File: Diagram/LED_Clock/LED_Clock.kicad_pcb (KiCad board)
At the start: 2 copper layers, 190.5 x 159.4 mm, 79 parts, among them SW1 SW_Push_Dual, U1 ATmega328P-PU, U2 DS3231MZ, U3 MCP23017-E_SP, U4 MCP23017-E_SP, U5 Barreljack, U6 JST4pin, Y1 Crystal

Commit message: Ground Plane
added a Ground plane and some missing traces.
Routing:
- net Net-(D9-Pad1): track 0.00 -> 10.2 mm
- net Net-(D8-Pad1): track 0.00 -> 10.2 mm
- net Net-(D7-Pad1): track 0.00 -> 10.2 mm
- net Net-(D6-Pad1): track 0.00 -> 10.2 mm
- net Net-(D5-Pad1): track 0.00 -> 10.2 mm
- net Net-(D15-Pad1): track 0.00 -> 10.2 mm
- net Net-(D14-Pad1): track 0.00 -> 10.2 mm
- net Net-(D13-Pad1): track 0.00 -> 10.2 mm
- net Net-(D12-Pad1): track 0.00 -> 10.2 mm
- net Net-(D11-Pad1): track 0.00 -> 10.2 mm
- net Net-(D10-Pad1): track 0.00 -> 10.2 mm
- added copper zone on F.Cu, net GND

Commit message: updated
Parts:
- moved R1 34.9 mm to (84.8, 128.5), turned to 270 degrees
- moved SW1 28.5 mm to (77.2, 131.6)
- moved REF** 25.3 mm to (60.5, 146.8)
- moved U5 23.6 mm to (58.9, 130.6)
- moved U1 22.5 mm to (144.3, 108.7)
- moved Y1 22.0 mm to (138.2, 130.6)
- moved REF** 21.0 mm to (214.4, 146.8)
- moved C1 20.8 mm to (133.1, 133.1)
- moved C2 20.7 mm to (133.1, 128.0)
- moved R2 20.0 mm to (158.2, 110.7)
- moved R3 20.0 mm to (158.2, 115.8)
- moved REF** 19.8 mm to (177.6, 129.0)
- moved REF** 19.8 mm to (177.5, 122.0)
- moved U2 19.8 mm to (159.8, 124.7)
- moved REF** 19.6 mm to (60.5, 29.5)
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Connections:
- net GPB1 renamed Net-(R16-Pad2)
- R15 pad 2: GPB0 -> Net-(R15-Pad2)
- R17 pad 2: GPB2 -> Net-(R17-Pad2)
- R18 pad 2: GPB3 -> Net-(R18-Pad2)
- R19 pad 2: GPB4 -> Net-(R19-Pad2)
- R20 pad 2: GPB5 -> Net-(R20-Pad2)
- R21 pad 2: GPB6 -> Net-(R21-Pad2)
- R30 pad 2: HGPB0 -> Net-(R30-Pad2)
- R31 pad 2: HGPB1 -> Net-(R31-Pad2)
- R32 pad 2: HGPB2 -> Net-(R32-Pad2)
- R33 pad 2: HGPB3 -> Net-(R33-Pad2)
- U1 pad 16: Net-(U1-Pad16) -> +5V
- U1 pad 18: Net-(U1-Pad18) -> GND
- U3 pad 1: GPB0 -> Net-(R17-Pad2)
- U3 pad 21: Net-(R7-Pad2) -> Net-(R10-Pad2)
- U3 pad 22: Net-(R8-Pad2) -> Net-(R9-Pad2)
- U3 pad 23: Net-(R9-Pad2) -> Net-(R8-Pad2)
- U3 pad 24: Net-(R10-Pad2) -> Net-(R7-Pad2)
- U3 pad 25: Net-(R11-Pad2) -> Net-(R21-Pad2)
- U3 pad 26: Net-(R12-Pad2) -> Net-(R20-Pad2)
- U3 pad 27: Net-(R13-Pad2) -> Net-(R19-Pad2)
- U3 pad 28: Net-(R14-Pad2) -> Net-(R18-Pad2)
- U3 pad 3: GPB2 -> Net-(R15-Pad2)
- U3 pad 4: GPB3 -> Net-(R14-Pad2)
- U3 pad 5: GPB4 -> Net-(R13-Pad2)
- U3 pad 6: GPB5 -> Net-(R12-Pad2)
- U3 pad 7: GPB6 -> Net-(R11-Pad2)
- U4 pad 1: HGPB0 -> Net-(R25-Pad2)
- U4 pad 2: HGPB1 -> Net-(R24-Pad2)
- U4 pad 21: Net-(R22-Pad2) -> Net-(R33-Pad2)
- U4 pad 22: Net-(R23-Pad2) -> Net-(R32-Pad2)
- U4 pad 23: Net-(R24-Pad2) -> Net-(R31-Pad2)
- U4 pad 24: Net-(R25-Pad2) -> Net-(R30-Pad2)
- U4 pad 25: Net-(R26-Pad2) -> Net-(R29-Pad2)
- U4 pad 26: Net-(R27-Pad2) -> Net-(R28-Pad2)
- U4 pad 27: Net-(R28-Pad2) -> Net-(R27-Pad2)
- U4 pad 28: Net-(R29-Pad2) -> Net-(R26-Pad2)
- U4 pad 3: HGPB2 -> Net-(R23-Pad2)
- U4 pad 4: HGPB3 -> Net-(R22-Pad2)
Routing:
- net Net-(R33-Pad2): track 0.00 -> 172.7 mm
- net GND: track 1150.4 -> 982.4 mm
- net Net-(R32-Pad2): track 0.00 -> 158.5 mm
- net Net-(R21-Pad2): track 0.00 -> 151.5 mm
- net HGPB3: track 149.6 -> 0.00 mm
- net Net-(R31-Pad2): track 0.00 -> 144.4 mm
- net Net-(R20-Pad2): track 0.00 -> 137.4 mm
- net HGPB2: track 135.8 -> 0.00 mm
- net GPB6: track 130.3 -> 0.00 mm
- net Net-(R30-Pad2): track 0.00 -> 130.3 mm
- net /clock minute/SDA: track 261.5 -> 386.0 mm
- net Net-(R19-Pad2): track 0.00 -> 123.4 mm
- net HGPB1: track 122.0 -> 0.00 mm
- net GPB5: track 120.8 -> 0.00 mm
- net GPB2: track 115.4 -> 0.00 mm
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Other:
- board size 190.5 x 159.4 mm -> 164.1 x 127.5 mm
- rule pad_to_mask_clearance: 0.051 -> 0.00129
- rule solder_mask_min_width: 0.25 -> 0.002565
- rule trace_min: 0.2 -> 0.000152
- rule via_min_drill: 0.3 -> 0.000254
- rule via_min_size: 0.4 -> 0.000508

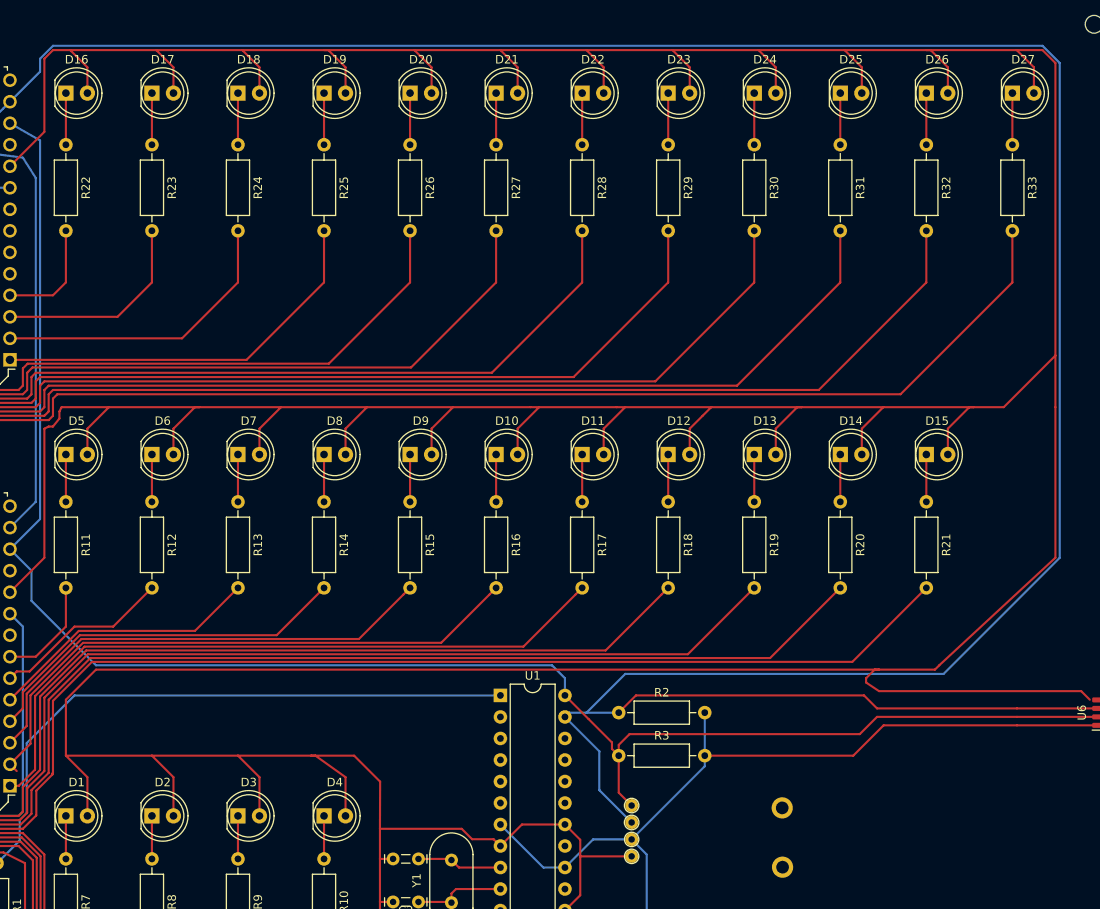
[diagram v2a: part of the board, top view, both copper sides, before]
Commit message: Updated
led flipped the RTS symbol remade and JST4pin enlarged
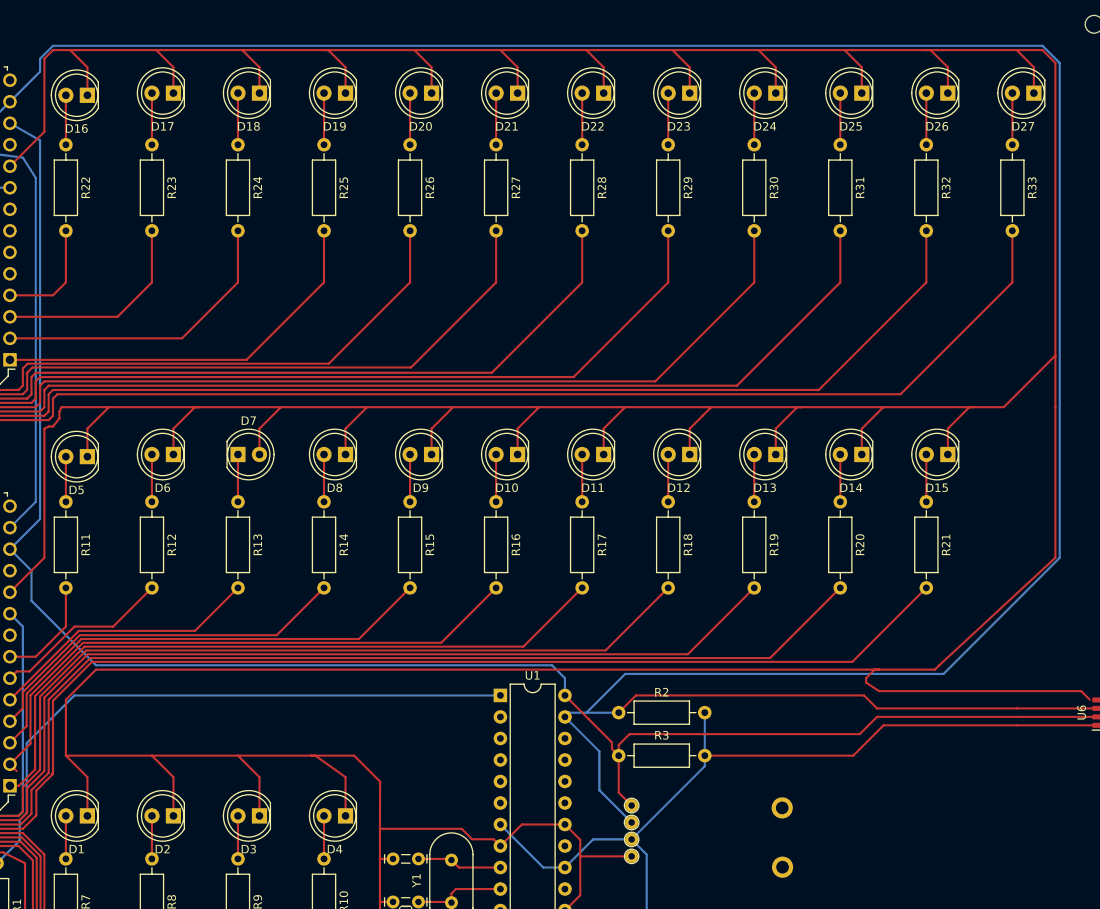
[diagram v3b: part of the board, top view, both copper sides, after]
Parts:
- moved D5 2.55 mm to (95.5, 80.5), turned to 180 degrees
- moved D16 2.55 mm to (95.5, 37.8), turned to 180 degrees
- moved D15 2.54 mm to (197.1, 80.3), turned to 180 degrees
- moved D26 2.54 mm to (197.1, 37.6), turned to 180 degrees
- moved D27 2.54 mm to (207.3, 37.6), turned to 180 degrees
- moved D1 2.54 mm to (95.5, 122.9), turned to 180 degrees
- moved D17 2.54 mm to (105.7, 37.6), turned to 180 degrees
- moved D2 2.54 mm to (105.7, 122.9), turned to 180 degrees
- moved D6 2.54 mm to (105.7, 80.3), turned to 180 degrees
- moved D10 2.54 mm to (146.3, 80.3), turned to 180 degrees
- moved D11 2.54 mm to (156.5, 80.3), turned to 180 degrees
- moved D12 2.54 mm to (166.6, 80.3), turned to 180 degrees
- moved D13 2.54 mm to (176.8, 80.3), turned to 180 degrees
- moved D14 2.54 mm to (186.9, 80.3), turned to 180 degrees
- moved D18 2.54 mm to (115.8, 37.6), turned to 180 degrees
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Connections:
- D1 pad 1: Net-(D1-Pad1) -> GND
- D1 pad 2: GND -> Net-(D1-Pad2)
- D10 pad 1: Net-(D10-Pad1) -> GND
- D10 pad 2: GND -> Net-(D10-Pad2)
- D11 pad 1: Net-(D11-Pad1) -> GND
- D11 pad 2: GND -> Net-(D11-Pad2)
- D12 pad 1: Net-(D12-Pad1) -> GND
- D12 pad 2: GND -> Net-(D12-Pad2)
- D13 pad 1: Net-(D13-Pad1) -> GND
- D13 pad 2: GND -> Net-(D13-Pad2)
- D14 pad 1: Net-(D14-Pad1) -> GND
- D14 pad 2: GND -> Net-(D14-Pad2)
- D15 pad 1: Net-(D15-Pad1) -> GND
- D15 pad 2: GND -> Net-(D15-Pad2)
- D16 pad 1: Net-(D16-Pad1) -> GND
- D16 pad 2: GND -> Net-(D16-Pad2)
- D17 pad 1: Net-(D17-Pad1) -> GND
- D17 pad 2: GND -> Net-(D17-Pad2)
- D18 pad 1: Net-(D18-Pad1) -> GND
- D18 pad 2: GND -> Net-(D18-Pad2)
- D19 pad 1: Net-(D19-Pad1) -> GND
- D19 pad 2: GND -> Net-(D19-Pad2)
- D2 pad 1: Net-(D2-Pad1) -> GND
- D2 pad 2: GND -> Net-(D2-Pad2)
- D20 pad 1: Net-(D20-Pad1) -> GND
- D20 pad 2: GND -> Net-(D20-Pad2)
- D21 pad 1: Net-(D21-Pad1) -> GND
- D21 pad 2: GND -> Net-(D21-Pad2)
- D22 pad 1: Net-(D22-Pad1) -> GND
- D22 pad 2: GND -> Net-(D22-Pad2)
- D23 pad 1: Net-(D23-Pad1) -> GND
- D23 pad 2: GND -> Net-(D23-Pad2)
- D24 pad 1: Net-(D24-Pad1) -> GND
- D24 pad 2: GND -> Net-(D24-Pad2)
- D25 pad 1: Net-(D25-Pad1) -> GND
- D25 pad 2: GND -> Net-(D25-Pad2)
- D26 pad 1: Net-(D26-Pad1) -> GND
- D26 pad 2: GND -> Net-(D26-Pad2)
- D27 pad 1: Net-(D27-Pad1) -> GND
- D27 pad 2: GND -> Net-(D27-Pad2)
- D3 pad 1: Net-(D3-Pad1) -> GND
- D3 pad 2: GND -> Net-(D3-Pad2)
- D4 pad 1: Net-(D4-Pad1) -> GND
- D4 pad 2: GND -> Net-(D4-Pad2)
- D5 pad 1: Net-(D5-Pad1) -> GND
- D5 pad 2: GND -> Net-(D5-Pad2)
- D6 pad 1: Net-(D6-Pad1) -> GND
- D6 pad 2: GND -> Net-(D6-Pad2)
- D7 pad 1: Net-(D7-Pad1) -> GND
- D7 pad 2: GND -> Net-(D7-Pad2)
- D8 pad 1: Net-(D8-Pad1) -> GND
- D8 pad 2: GND -> Net-(D8-Pad2)
- D9 pad 1: Net-(D9-Pad1) -> GND
- D9 pad 2: GND -> Net-(D9-Pad2)
- R10 pad 1: Net-(D4-Pad1) -> Net-(D4-Pad2)
- R11 pad 1: Net-(D5-Pad1) -> Net-(D5-Pad2)
- R12 pad 1: Net-(D6-Pad1) -> Net-(D6-Pad2)
- R13 pad 1: Net-(D7-Pad1) -> Net-(D7-Pad2)
- R14 pad 1: Net-(D8-Pad1) -> Net-(D8-Pad2)
- R15 pad 1: Net-(D9-Pad1) -> Net-(D9-Pad2)
- R16 pad 1: Net-(D10-Pad1) -> Net-(D10-Pad2)
- R17 pad 1: Net-(D11-Pad1) -> Net-(D11-Pad2)
- R18 pad 1: Net-(D12-Pad1) -> Net-(D12-Pad2)
- R19 pad 1: Net-(D13-Pad1) -> Net-(D13-Pad2)
- R20 pad 1: Net-(D14-Pad1) -> Net-(D14-Pad2)
- R21 pad 1: Net-(D15-Pad1) -> Net-(D15-Pad2)
- R22 pad 1: Net-(D16-Pad1) -> Net-(D16-Pad2)
- R23 pad 1: Net-(D17-Pad1) -> Net-(D17-Pad2)
- R24 pad 1: Net-(D18-Pad1) -> Net-(D18-Pad2)
- R25 pad 1: Net-(D19-Pad1) -> Net-(D19-Pad2)
- R26 pad 1: Net-(D20-Pad1) -> Net-(D20-Pad2)
- R27 pad 1: Net-(D21-Pad1) -> Net-(D21-Pad2)
- R28 pad 1: Net-(D22-Pad1) -> Net-(D22-Pad2)
- R29 pad 1: Net-(D23-Pad1) -> Net-(D23-Pad2)
- R30 pad 1: Net-(D24-Pad1) -> Net-(D24-Pad2)
- R31 pad 1: Net-(D25-Pad1) -> Net-(D25-Pad2)
- R32 pad 1: Net-(D26-Pad1) -> Net-(D26-Pad2)
- R33 pad 1: Net-(D27-Pad1) -> Net-(D27-Pad2)
- R7 pad 1: Net-(D1-Pad1) -> Net-(D1-Pad2)
- R8 pad 1: Net-(D2-Pad1) -> Net-(D2-Pad2)
- R9 pad 1: Net-(D3-Pad1) -> Net-(D3-Pad2)
- U1 pad 16: +5V -> Net-(U1-Pad16)
- U1 pad 18: GND -> Net-(U1-Pad18)
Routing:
- net Net-(D27-Pad2): track 0.00 -> 6.10 mm
- net Net-(D27-Pad1): track 6.10 -> 0.00 mm
- net Net-(D26-Pad2): track 0.00 -> 6.10 mm
- net Net-(D26-Pad1): track 6.10 -> 0.00 mm
- net Net-(D25-Pad2): track 0.00 -> 6.10 mm
- net Net-(D25-Pad1): track 6.10 -> 0.00 mm
- net Net-(D24-Pad2): track 0.00 -> 6.10 mm
- net Net-(D24-Pad1): track 6.10 -> 0.00 mm
- net Net-(D23-Pad2): track 0.00 -> 6.10 mm
- net Net-(D23-Pad1): track 6.10 -> 0.00 mm
- net Net-(D22-Pad2): track 0.00 -> 6.10 mm
- net Net-(D22-Pad1): track 6.10 -> 0.00 mm
- net Net-(D21-Pad2): track 0.00 -> 6.10 mm
- net Net-(D21-Pad1): track 6.10 -> 0.00 mm
- net Net-(D20-Pad2): track 0.00 -> 6.10 mm
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
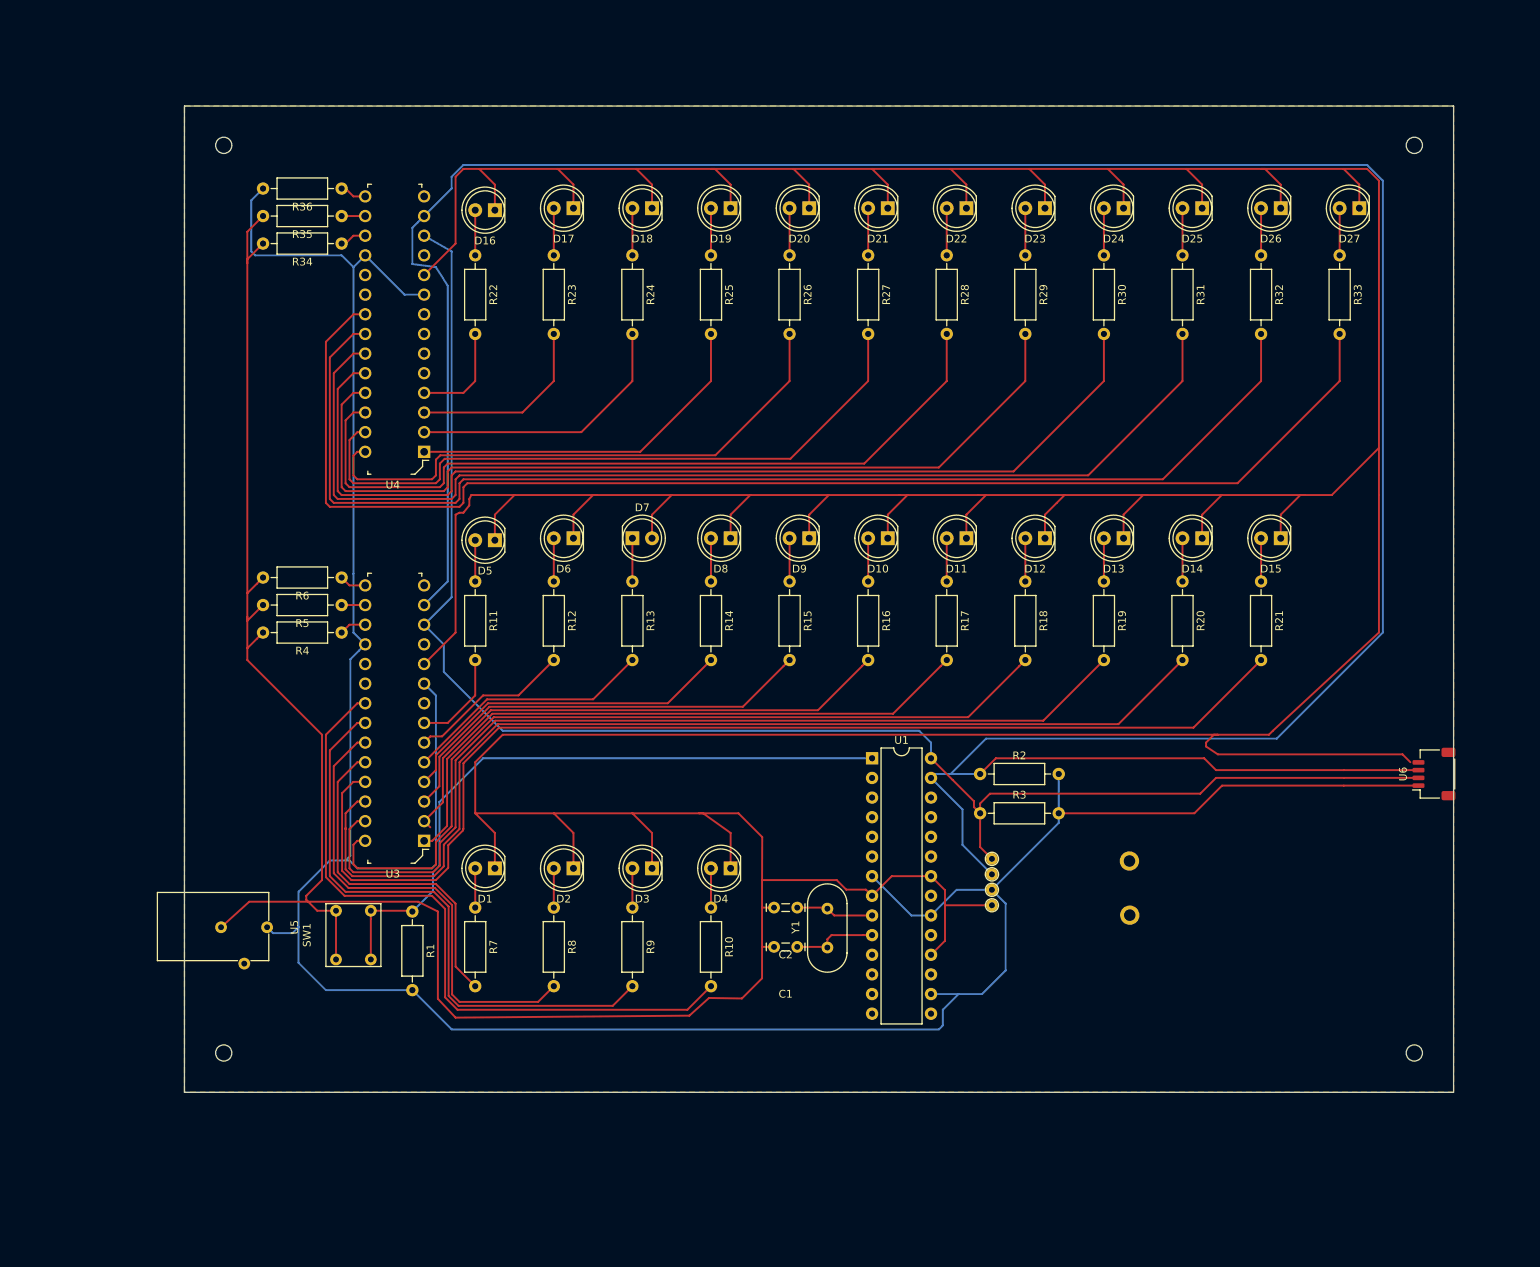
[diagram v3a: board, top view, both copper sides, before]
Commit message: update 1.2
new mounting holes jst4 pin mounting points to ground and refilled
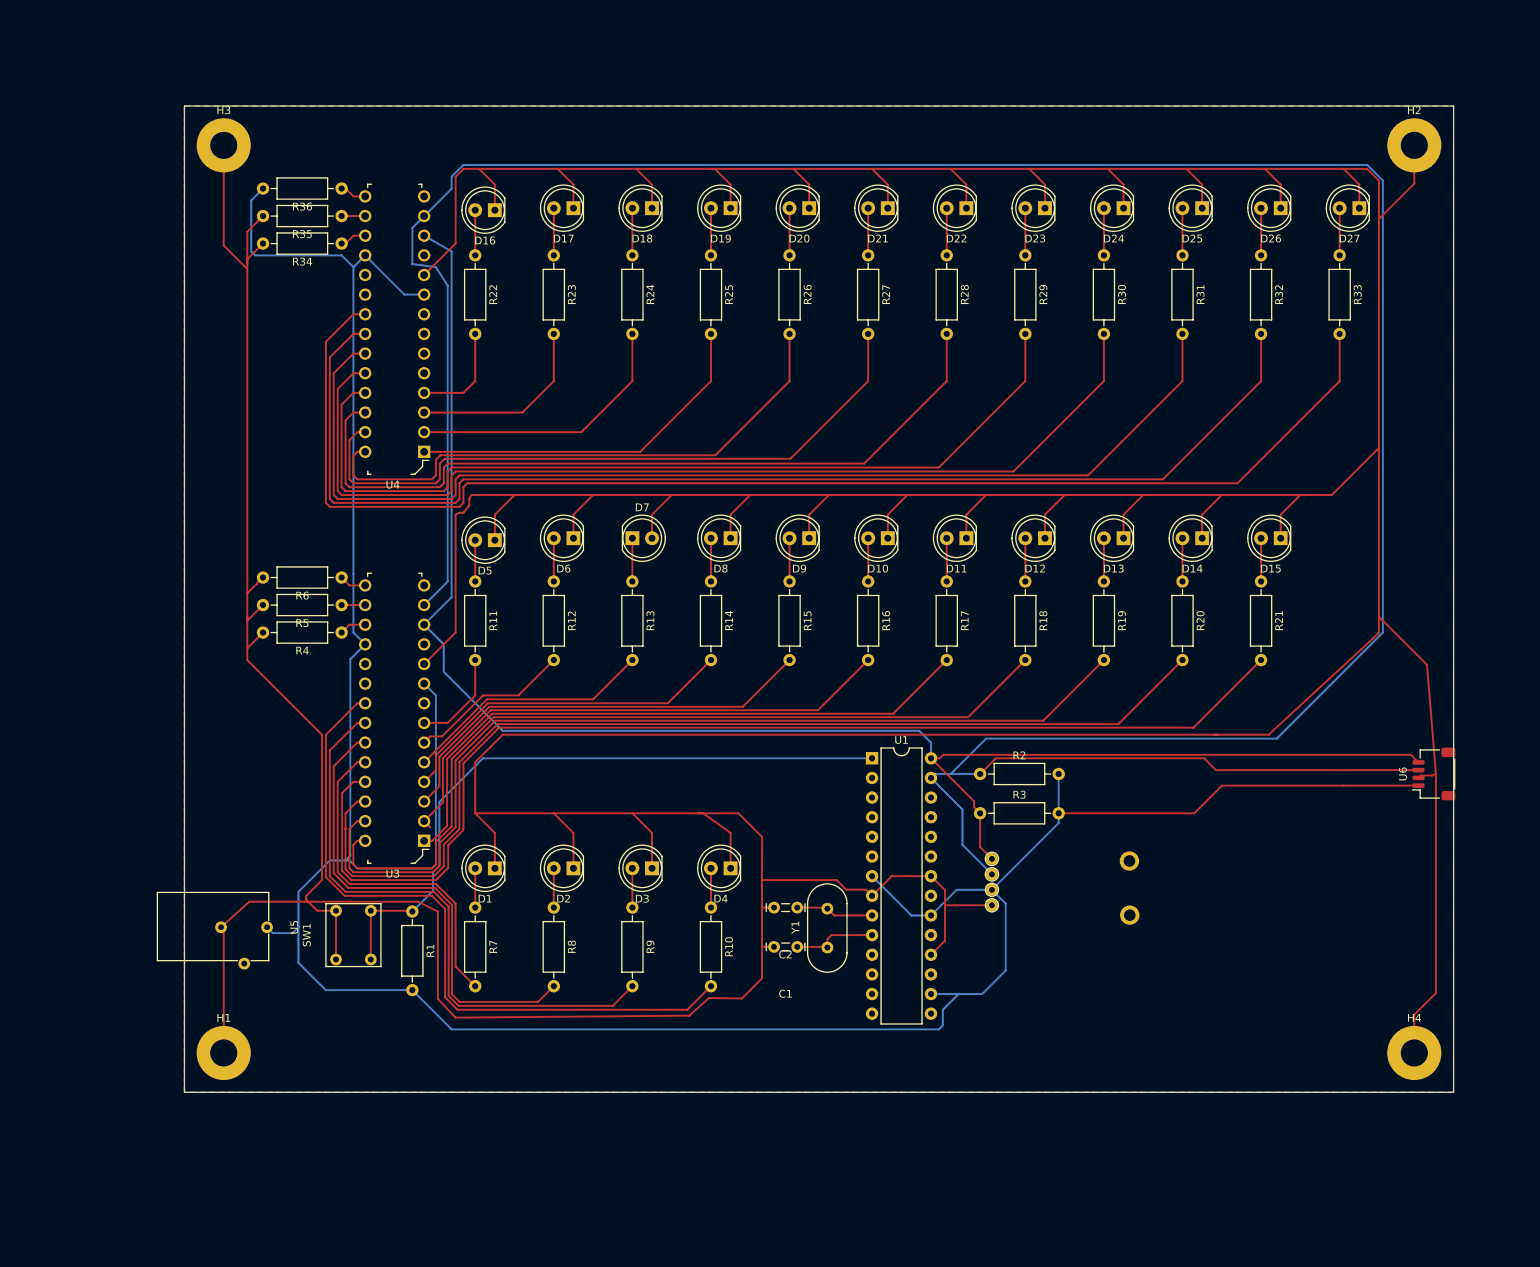
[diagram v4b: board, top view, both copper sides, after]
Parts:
- removed the REF** at (60.5, 146.8)
- removed the REF** at (60.5, 29.5)
- removed the REF** at (214.4, 146.8)
- removed the REF** at (214.4, 29.5)
- added H1: MountingHole_Pad, MountingHole:MountingHole_3.5mm_Pad, F.Cu at (60.5, 146.8)
- added H2: MountingHole_Pad, MountingHole:MountingHole_3.5mm_Pad, F.Cu at (214.4, 29.5)
- added H3: MountingHole_Pad, MountingHole:MountingHole_3.5mm_Pad, F.Cu at (60.5, 29.5)
- added H4: MountingHole_Pad, MountingHole:MountingHole_3.5mm_Pad, F.Cu at (214.4, 146.8)
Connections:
- U6 pad 2: /clock minute/SCL -> GND
- U6 pad 4: GND -> /clock minute/SCL
- U6 pad MP: (no net) -> GND
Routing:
- net GND: track 982.4 -> 1060.9 mm
- net /clock minute/SCL: track 205.4 -> 209.7 mm
